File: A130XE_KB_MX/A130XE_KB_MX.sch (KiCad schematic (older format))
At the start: 75 parts, among them J1 34 pin RIBBON KEYBOARD CABLE, J2 Conn_01x02_Male, SW1 KS_RESET, SW10 K_5, SW11 K_I, SW12 K_T, SW13 K_G, SW14 K_SPACE, SW15 K_B, SW16 K_K, SW17 KS_SELECT, SW18 K_4, SW19 K_O, SW2 K_6, SW20 K_R, SW21 K_F, SW22 K_M, SW23 K_V, SW24 K_L, SW25 K_3, SW26 K_P, SW27 K_E, SW28 K_D, SW29 KS_START, SW3 K_U, SW30 K_comma, SW31 K_comdot, SW32 K_C, SW33 K_dot, SW34 K_2, SW35 K_minus, SW36 K_W, SW37 K_S, SW38 K_X, SW39 K_plus, SW4 K_Y, SW40 K_1, SW41 K_equal, SW42 K_Q, SW43 K_A, SW44 K_slash, SW45 K_asterisk, SW46 K_Z, SW47 K_ATARI, SW48 K_ESC, SW49 K_RETURN, SW5 K_H, SW50 K_TAB, SW51 K_CAPS, SW52 K_CTRL, SW53 K_LSHIFT, SW54 K_RSHIFT, SW55 K_BRK, SW56 K_DEL, SW57 K_GT, SW58 K_LT, SW59 K_0, SW6 K_N, SW60 K_9, SW61 K_8, SW62 K_7, SW63 K_SPACE_1, SW64 K_SPACE_2, SW65 K_F1, SW66 K_F2, SW67 K_F3, SW68 K_F4, SW7 KS_HELP, SW8 K_J, SW9 KS_OPTION

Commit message: New layout for spacebar 6.25 and two 1.25 at side. Function keys are 1.5u.
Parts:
- SW1, SW17, SW29, SW7, SW9: footprint Button_Switch_Keyboard:SW_Cherry_MX1A_1.00u_PCB -> Button_Switch_Keyboard:SW_Cherry_MX1A_1.50u_PCB
- SW63, SW64: footprint Button_Switch_Keyboard:SW_Cherry_MX1A_1.00u_PCB -> Button_Switch_Keyboard:SW_Cherry_MX1A_1.25u_PCB
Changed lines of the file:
@@
 Title "ATARI XE KEYBOARD PCB "
 Date "2020-10-10"
-Rev "0.1"
+Rev "0.2"
 Comp "RetroBitLab Tech Guy"
 Comment1 "A PCB KEYBOARD AS DROP IN REPLACEMENT"
@@
 F 0 "SW1" H 10700 3435 50  0000 C CNN
 F 1 "KS_RESET" H 10700 3344 50  0000 C CNN
-F 2 "Button_Switch_Keyboard:SW_Cherry_MX1A_1.00u_PCB" H 10700 3350 50  0001 C CNN
+F 2 "Button_Switch_Keyboard:SW_Cherry_MX1A_1.50u_PCB" H 10700 3350 50  0001 C CNN
 F 3 "" H 10700 3350 50  0001 C CNN
 	1    10700 3150
@@
 F 0 "SW9" H 11600 3435 50  0000 C CNN
 F 1 "KS_OPTION" H 11600 3344 50  0000 C CNN
-F 2 "Button_Switch_Keyboard:SW_Cherry_MX1A_1.00u_PCB" H 11600 3350 50  0001 C CNN
+F 2 "Button_Switch_Keyboard:SW_Cherry_MX1A_1.50u_PCB" H 11600 3350 50  0001 C CNN
 F 3 "" H 11600 3350 50  0001 C CNN
 	1    11600 3150
@@
 F 0 "SW17" H 12500 3435 50  0000 C CNN
 F 1 "KS_SELECT" H 12500 3344 50  0000 C CNN
-F 2 "Button_Switch_Keyboard:SW_Cherry_MX1A_1.00u_PCB" H 12500 3350 50  0001 C CNN
+F 2 "Button_Switch_Keyboard:SW_Cherry_MX1A_1.50u_PCB" H 12500 3350 50  0001 C CNN
 F 3 "" H 12500 3350 50  0001 C CNN
 	1    12500 3150
@@
 F 0 "SW29" H 13350 3435 50  0000 C CNN
 F 1 "KS_START" H 13350 3344 50  0000 C CNN
-F 2 "Button_Switch_Keyboard:SW_Cherry_MX1A_1.00u_PCB" H 13350 3350 50  0001 C CNN
+F 2 "Button_Switch_Keyboard:SW_Cherry_MX1A_1.50u_PCB" H 13350 3350 50  0001 C CNN
 F 3 "" H 13350 3350 50  0001 C CNN
 	1    13350 3150
@@
 F 0 "SW7" H 2450 10335 50  0000 C CNN
 F 1 "KS_HELP" H 2450 10244 50  0000 C CNN
-F 2 "Button_Switch_Keyboard:SW_Cherry_MX1A_1.00u_PCB" H 2450 10250 50  0001 C CNN
+F 2 "Button_Switch_Keyboard:SW_Cherry_MX1A_1.50u_PCB" H 2450 10250 50  0001 C CNN
 F 3 "" H 2450 10250 50  0001 C CNN
 	1    2450 10050
@@
 F 0 "SW63" H 3350 9201 50  0000 C CNN
 F 1 "K_SPACE_1" H 3350 9127 28  0000 C CNN
-F 2 "Button_Switch_Keyboard:SW_Cherry_MX1A_1.00u_PCB" H 3350 9150 50  0001 C CNN
+F 2 "Button_Switch_Keyboard:SW_Cherry_MX1A_1.25u_PCB" H 3350 9150 50  0001 C CNN
 F 3 "" H 3350 9150 50  0001 C CNN
 	1    3350 8950
@@
 F 0 "SW64" H 3350 9551 50  0000 C CNN
 F 1 "K_SPACE_2" H 3350 9477 28  0000 C CNN
-F 2 "Button_Switch_Keyboard:SW_Cherry_MX1A_1.00u_PCB" H 3350 9500 50  0001 C CNN
+F 2 "Button_Switch_Keyboard:SW_Cherry_MX1A_1.25u_PCB" H 3350 9500 50  0001 C CNN
 F 3 "" H 3350 9500 50  0001 C CNN
 	1    3350 9300

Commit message: Changed layout of buttons surrounding the spacebar. Atari XE seems to have 9U spacebar, so we are using 6.25u (more common) and two keys around it (1.25u and 1.50u)
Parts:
- SW64: footprint Button_Switch_Keyboard:SW_Cherry_MX1A_1.25u_PCB -> Button_Switch_Keyboard:SW_Cherry_MX1A_1.50u_PCB
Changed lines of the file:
@@
 F 0 "SW64" H 3350 9551 50  0000 C CNN
 F 1 "K_SPACE_2" H 3350 9477 28  0000 C CNN
-F 2 "Button_Switch_Keyboard:SW_Cherry_MX1A_1.25u_PCB" H 3350 9500 50  0001 C CNN
+F 2 "Button_Switch_Keyboard:SW_Cherry_MX1A_1.50u_PCB" H 3350 9500 50  0001 C CNN
 F 3 "" H 3350 9500 50  0001 C CNN
 	1    3350 9300

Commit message: Added new footprints for keys (with 3D WRL and Stabilizers where needed)
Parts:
- SW1, SW17, SW29, SW49, SW50, SW64, SW7, SW9: footprint Button_Switch_Keyboard:SW_Cherry_MX1A_1.50u_PCB -> RetroBitLab:SW_Cherry_MX1A_1.50u_PCB_3d
- SW10, SW11, SW12, SW13, SW15, SW16, SW18, SW19, SW2, SW20, SW21, SW22, SW23, SW24, SW25, SW26, SW27, SW28, SW3, SW30, SW31, SW32, SW33, SW34, SW35, SW36, SW37, SW38, SW39, SW4, SW40, SW41, SW42, SW43, SW44, SW45, SW46, SW47, SW48, SW5, SW55, SW56, SW57, SW58, SW59, SW6, SW60, SW61, SW62, SW65, SW66, SW67, SW68, SW8: footprint Button_Switch_Keyboard:SW_Cherry_MX1A_1.00u_PCB -> RetroBitLab:SW_Cherry_MX1A_1.00u_PCB_3d
- SW14: footprint Button_Switch_Keyboard:SW_Cherry_MX1A_6.25u_PCB -> RetroBitLab:SW_Cherry_MX1A_6.25u_PCB_3d
- SW51, SW63: footprint Button_Switch_Keyboard:SW_Cherry_MX1A_1.25u_PCB -> RetroBitLab:SW_Cherry_MX1A_1.25u_PCB_3d
- SW52, SW54: footprint Button_Switch_Keyboard:SW_Cherry_MX1A_1.75u_PCB -> RetroBitLab:SW_Cherry_MX1A_1.75u_PCB_3d
- SW53: footprint Button_Switch_Keyboard:SW_Cherry_MX1A_2.25u_PCB -> RetroBitLab:SW_Cherry_MX1A_2.25u_PCB_3d

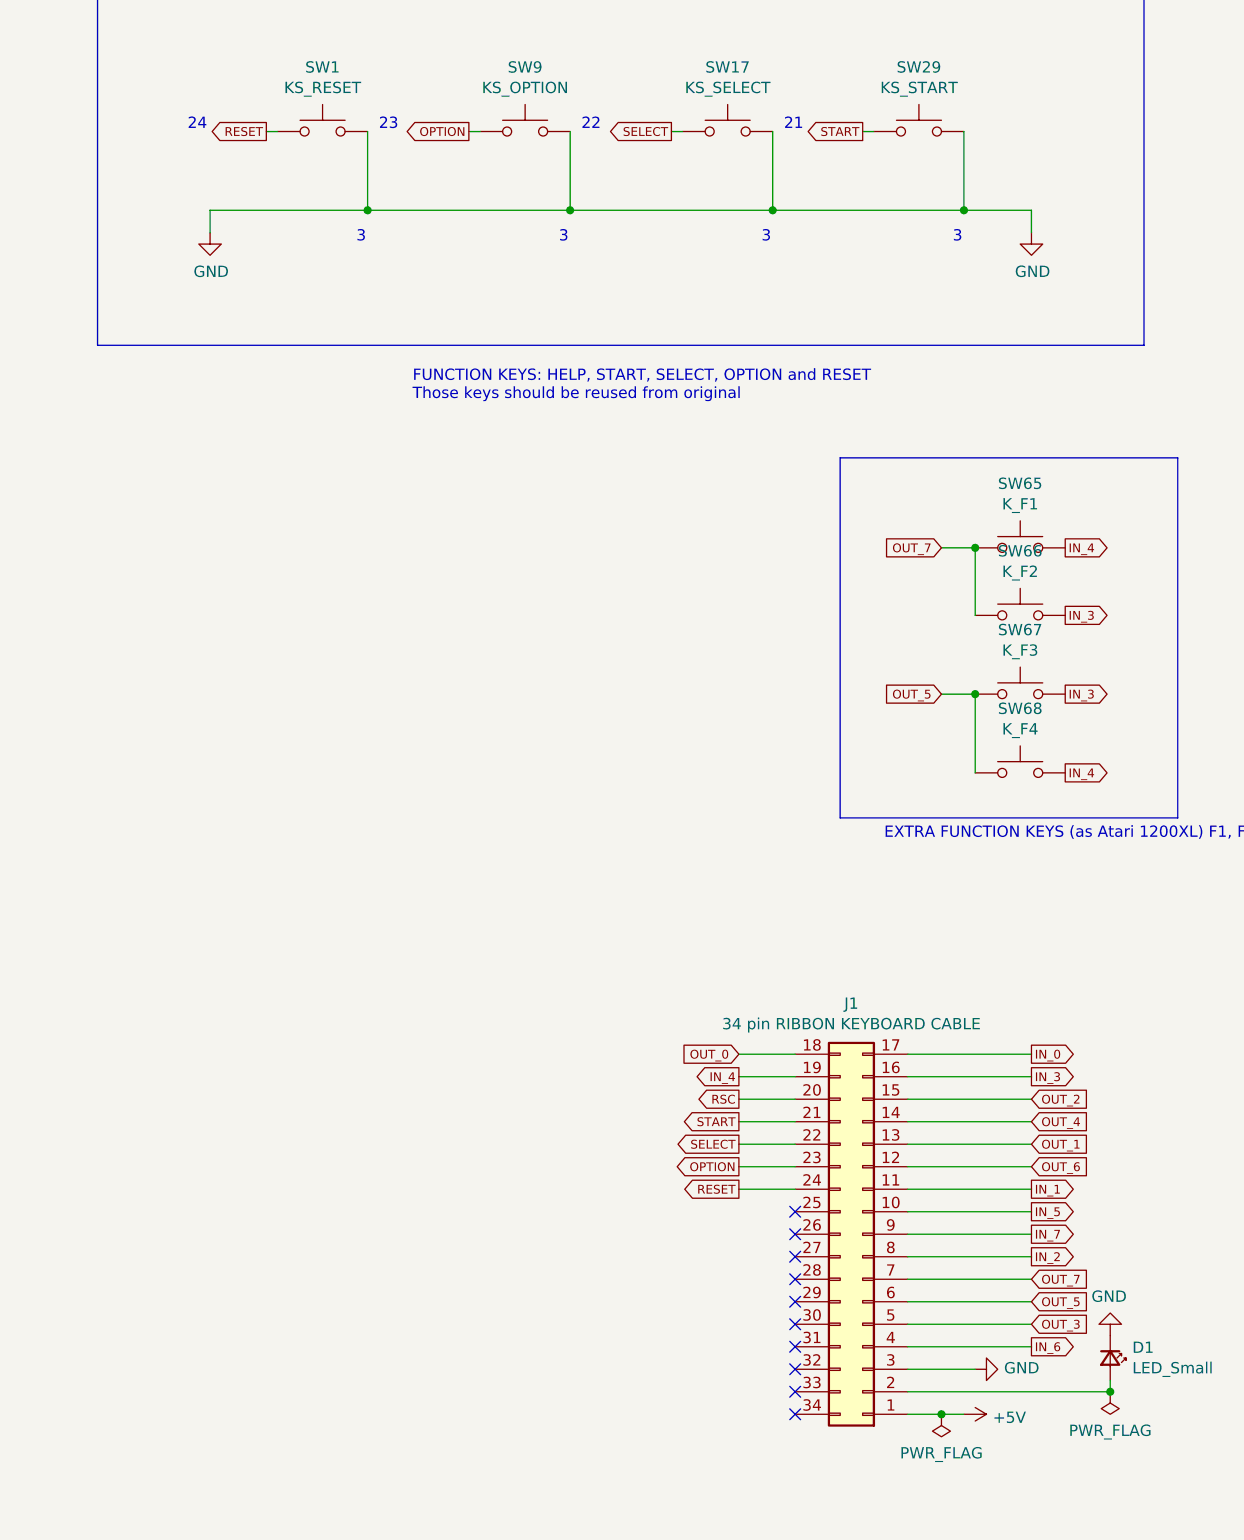
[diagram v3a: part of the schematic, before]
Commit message: F3 and F4 were inverted. Now they works fine. Thanks to OS ROM SELF-TEST Keyboard test.
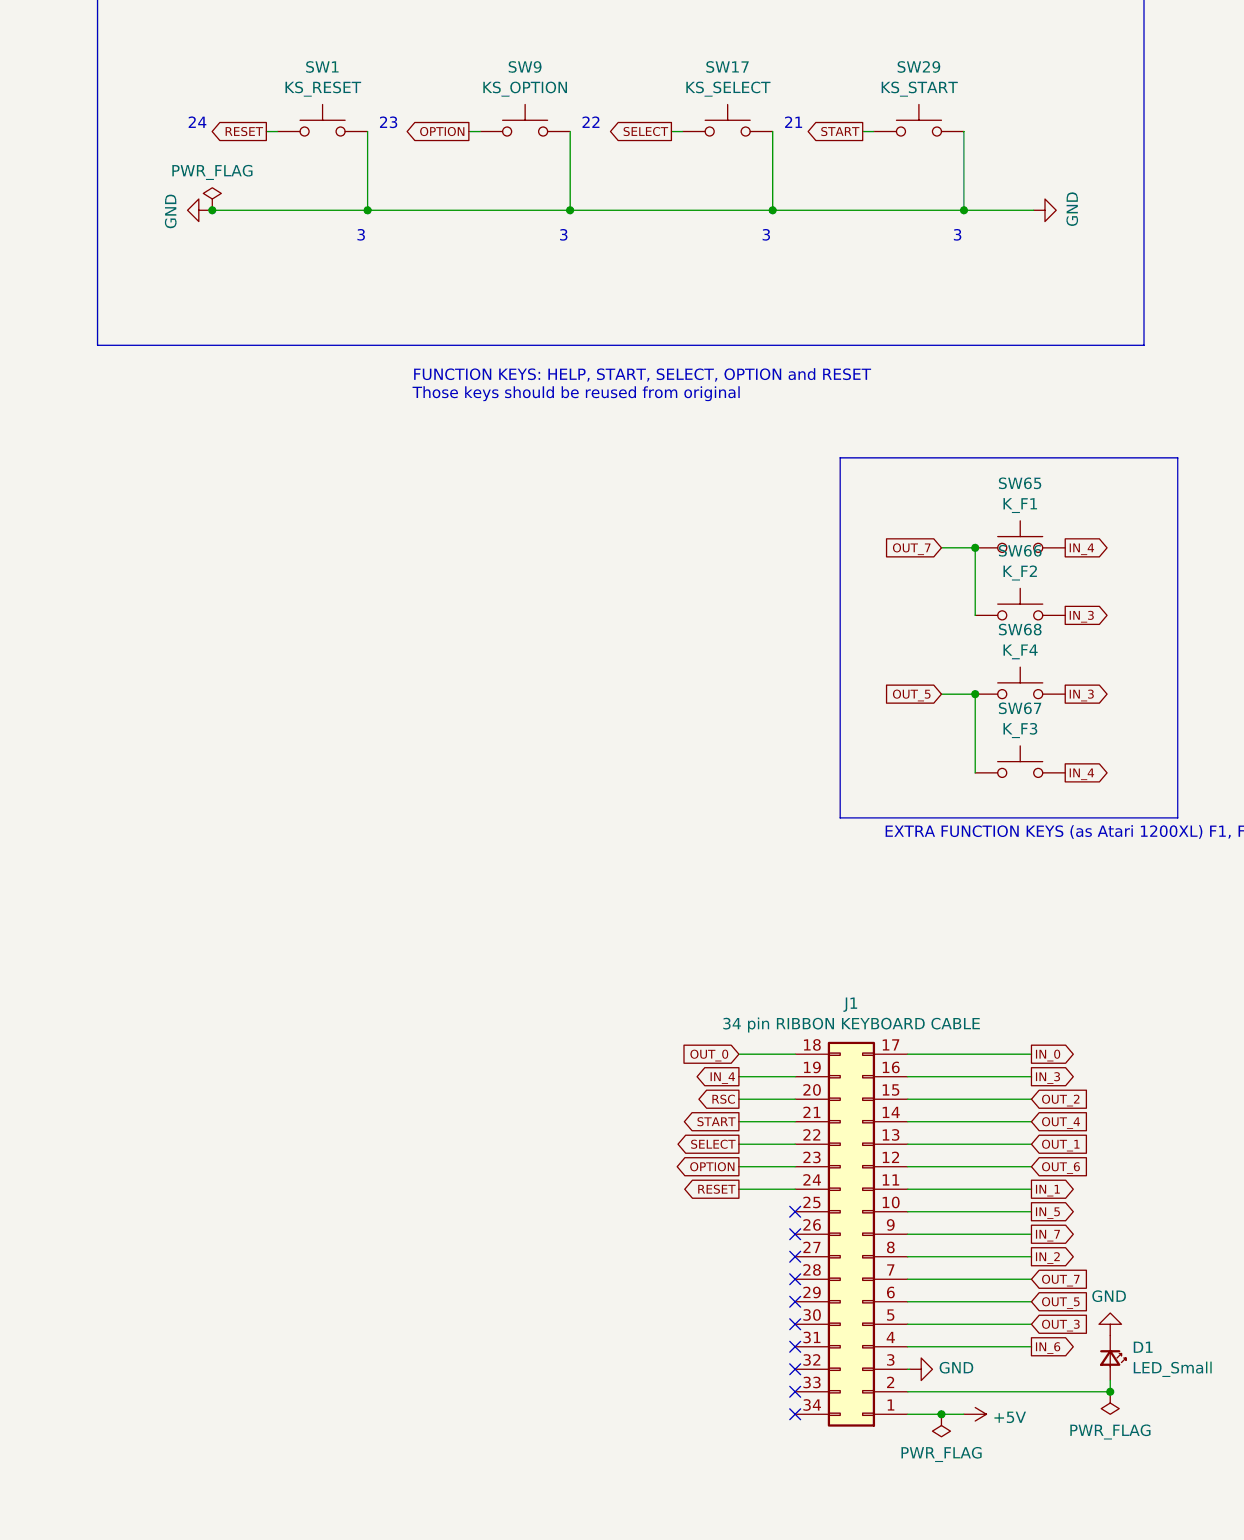
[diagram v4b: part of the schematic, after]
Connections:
- net IN_3: now also SW68.2; no longer SW67.2
- net IN_4: now also SW67.2; no longer SW68.2
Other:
- moved on the sheet: SW67, SW68
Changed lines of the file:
@@
 Sheet 1 1
 Title "ATARI XE KEYBOARD PCB "
-Date "2020-10-10"
-Rev "0.2"
+Date "2021-01-30"
+Rev "2.0"
 Comp "RetroBitLab Tech Guy"
 Comment1 "A PCB KEYBOARD AS DROP IN REPLACEMENT"
@@
 L power:GND #PWR04
 U 1 1 5F820F2B
-P 13600 8650
-F 0 "#PWR04" H 13600 8400 50  0001 C CNN
-F 1 "GND" V 13605 8522 50  0000 R CNN
-F 2 "" H 13600 8650 50  0001 C CNN
-F 3 "" H 13600 8650 50  0001 C CNN
-	1    13600 8650
+P 13310 8650
+F 0 "#PWR04" H 13310 8400 50  0001 C CNN
+F 1 "GND" V 13315 8522 50  0000 R CNN
+F 2 "" H 13310 8650 50  0001 C CNN
+F 3 "" H 13310 8650 50  0001 C CNN
+	1    13310 8650
 	0    -1   -1   0
 $EndComp
@@
 L power:GND #PWR02
 U 1 1 5F826B7B
-P 13850 3600
-F 0 "#PWR02" H 13850 3350 50  0001 C CNN
-F 1 "GND" H 13855 3427 50  0000 C CNN
-F 2 "" H 13850 3600 50  0001 C CNN
-F 3 "" H 13850 3600 50  0001 C CNN
-	1    13850 3600
-	1    0    0    -1
+P 13860 3500
+F 0 "#PWR02" H 13860 3250 50  0001 C CNN
+F 1 "GND" H 13865 3327 50  0000 C CNN
+F 2 "" H 13860 3500 50  0001 C CNN
+F 3 "" H 13860 3500 50  0001 C CNN
+	1    13860 3500
+	0    -1   -1   0
 $EndComp
 $Comp
 L power:GND #PWR01
 U 1 1 5F826BB2
-P 10200 3600
-F 0 "#PWR01" H 10200 3350 50  0001 C CNN
-F 1 "GND" H 10205 3427 50  0000 C CNN
-F 2 "" H 10200 3600 50  0001 C CNN
-F 3 "" H 10200 3600 50  0001 C CNN
-	1    10200 3600
-	1    0    0    -1
+P 10200 3500
+F 0 "#PWR01" H 10200 3250 50  0001 C CNN
+F 1 "GND" H 10205 3327 50  0000 C CNN
+F 2 "" H 10200 3500 50  0001 C CNN
+F 3 "" H 10200 3500 50  0001 C CNN
+	1    10200 3500
+	0    1    1    0
 $EndComp
 $Comp
@@
 Text GLabel 7100 6250 2    39   Output ~ 0
 IN_0
-Wire Wire Line
-	13550 3500 13850 3500
 Connection ~ 13550 3500
 Wire Wire Line
@@
 OUT_4
 Wire Wire Line
-	13850 3500 13850 3600
-Wire Wire Line
 	14200 8750 14200 8700
 Wire Wire Line
-	13300 8650 13600 8650
-Wire Wire Line
-	10200 3600 10200 3500
-Wire Wire Line
-	10200 3500 10900 3500
+	10200 3500 10210 3500
 Text Notes 2250 10000 0    50   ~ 0
 6
@@
 L Switch:SW_Push SW67
 U 1 1 5F842671
+P 13800 6000
+F 0 "SW67" H 13800 6285 50  0000 C CNN
+F 1 "K_F3" H 13800 6194 50  0000 C CNN
+F 2 "RetroBitLab:SW_Cherry_MX1A_1.00u_PCB_3d" H 13800 6200 50  0001 C CNN
+F 3 "" H 13800 6200 50  0001 C CNN
+	1    13800 6000
+	1    0    0    -1
+$EndComp
+$Comp
+L Switch:SW_Push SW68
+U 1 1 5F84271F
 P 13800 5650
-F 0 "SW67" H 13800 5935 50  0000 C CNN
-F 1 "K_F3" H 13800 5844 50  0000 C CNN
+F 0 "SW68" H 13800 5935 50  0000 C CNN
+F 1 "K_F4" H 13800 5844 50  0000 C CNN
 F 2 "RetroBitLab:SW_Cherry_MX1A_1.00u_PCB_3d" H 13800 5850 50  0001 C CNN
 F 3 "" H 13800 5850 50  0001 C CNN
 	1    13800 5650
-	1    0    0    -1
-$EndComp
-$Comp
-L Switch:SW_Push SW68
-U 1 1 5F84271F
-P 13800 6000
-F 0 "SW68" H 13800 6285 50  0000 C CNN
-F 1 "K_F4" H 13800 6194 50  0000 C CNN
-F 2 "RetroBitLab:SW_Cherry_MX1A_1.00u_PCB_3d" H 13800 6200 50  0001 C CNN
-F 3 "" H 13800 6200 50  0001 C CNN
-	1    13800 6000
 	1    0    0    -1
 $EndComp
@@
 Text Notes 11100 4350 0    50   ~ 0
 FUNCTION KEYS: HELP, START, SELECT, OPTION and RESET\nThose keys should be reused from original
+Wire Wire Line
+	13550 3500 13860 3500
+Wire Wire Line
+	13300 8650 13310 8650
+$Comp
+L power:PWR_FLAG #FLG0101
+U 1 1 6020DE80
+P 10210 3500
+F 0 "#FLG0101" H 10210 3575 50  0001 C CNN
+F 1 "PWR_FLAG" H 10210 3674 50  0000 C CNN
+F 2 "" H 10210 3500 50  0001 C CNN
+F 3 "~" H 10210 3500 50  0001 C CNN
+	1    10210 3500
+	1    0    0    -1
+$EndComp
+Connection ~ 10210 3500
+Wire Wire Line
+	10210 3500 10900 3500
 $EndSCHEMATC
